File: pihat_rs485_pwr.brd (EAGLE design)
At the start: 56 x 65 mm, 36 parts, among them J1 RASPBERRYPI-40-PIN-GPIO_PTH_N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, Q1 MOSFET-N2N7002, Q2 MOSFET-N2N7002, Q3 MOSFET-N2N7002, Q4 MOSFET-P_SMD, Q5 BIPOLAR_TRANS_ARRAY, U1 MAX481CSA

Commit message: 11/29/17, changed PS, term blocks
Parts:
- 485: value TERMBLK_3PINNOSILK -> TERMBLK_3PINFEMALE; device UPenn:TERMBLK_3PIN_90_NOSILK -> UPenn:TERMBLK_FEMALE_3PIN_90_NOSILK
- J1: device UPenn:2X20 -> UPenn:PI_2X20
- PS1: value D24V22F5 -> R-78-E5.0; device UPenn:D24V22FX_FLAT -> UPenn:R-78-EXX
- moved S2 7.98 mm to (27.2, 21.3)
- moved R13 7.98 mm to (21.3, 23.1)
- moved R14 7.98 mm to (21.3, 19.6)
- moved R11 7.87 mm to (20.6, 34.0)
- moved R12 7.87 mm to (20.6, 28.7)
- moved 485 6.10 mm to (13.6, 27.9)
- moved RTCB 5.73 mm to (19.1, 16.0)
- moved R2 5.73 mm to (23.4, 16.0)
- moved R9 5.68 mm to (45.0, 22.6), turned to 0 degrees
- moved Q2 4.06 mm to (32.3, 27.7)
- moved R15 4.06 mm to (35.6, 36.8)
- moved C1 4.06 mm to (33.5, 17.3)
- moved Q1 4.06 mm to (45.7, 29.5)
- moved Q3 4.06 mm to (27.2, 27.7)
- moved R10 4.06 mm to (39.4, 36.3)
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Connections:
- net GND: now also 485.4
- net N$13: now also 485.5
- net N$25: now also 485.6
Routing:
- net N$27: track 19.1 -> 13.8 mm
- net N$3: track 53.4 -> 49.3 mm
- net N$22: track 56.9 -> 53.3 mm
- net N$2: track 16.0 -> 12.6 mm
- net 3.3V: track 89.7 -> 92.2 mm
- net N$25: track 31.6 -> 29.3 mm
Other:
- outline, holes or cut-outs redrawn
- board text added: "TX+"
- board text added: "TX-"
- board text removed: "EN"
- board text removed: "PG"

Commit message: 11/30/17, changes to silkscreen
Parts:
- moved PS1 2.54 mm to (17.8, 49.5)
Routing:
- net N$8: track 20.0 -> 17.4 mm
- net VIN: track 9.00 -> 11.4 mm
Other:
- board text added: "PIN11"
- board text added: "PIN15"
- board text added: "PIN15_CTRL"
- board text removed: "C"
- board text removed: "GPIO17"
- board text removed: "GPIO22"
- board text removed: "PIN_CTRL"

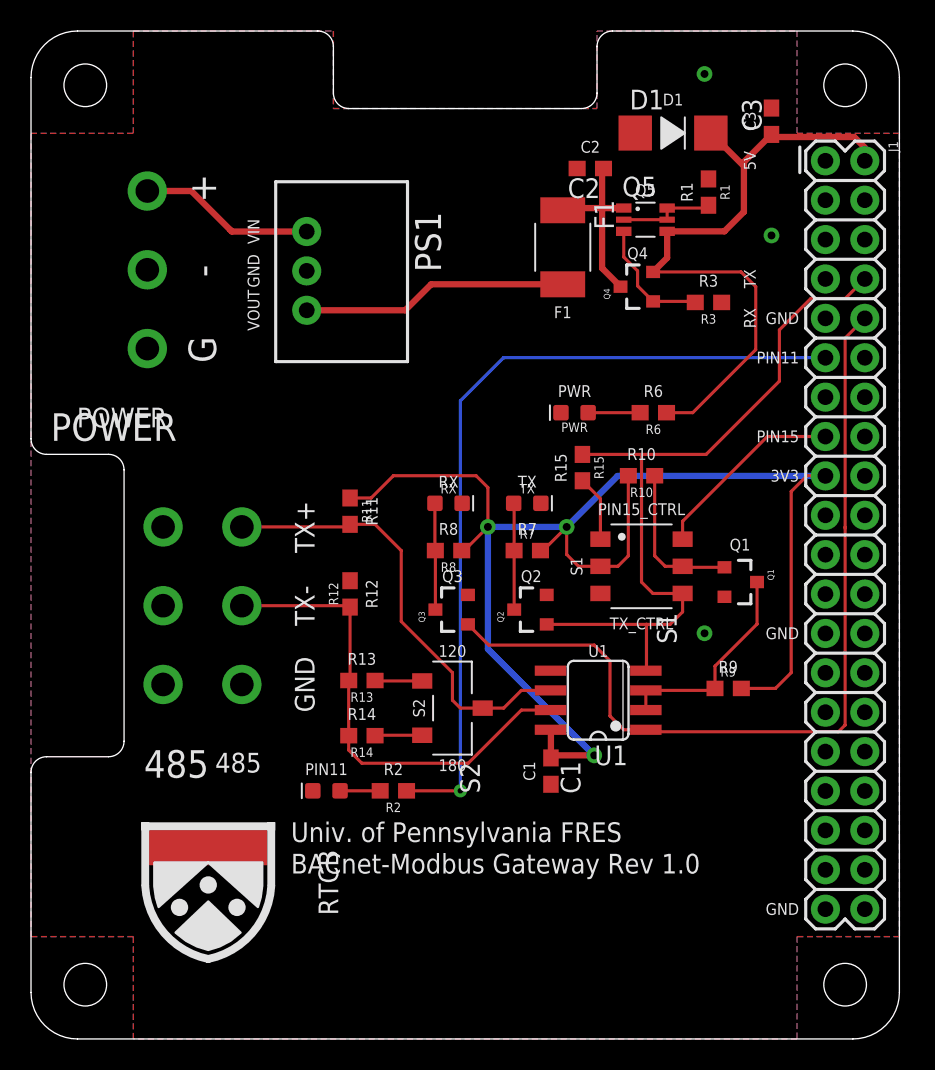
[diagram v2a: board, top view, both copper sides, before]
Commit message: 11/30/17, moved some parts, updated gerbers
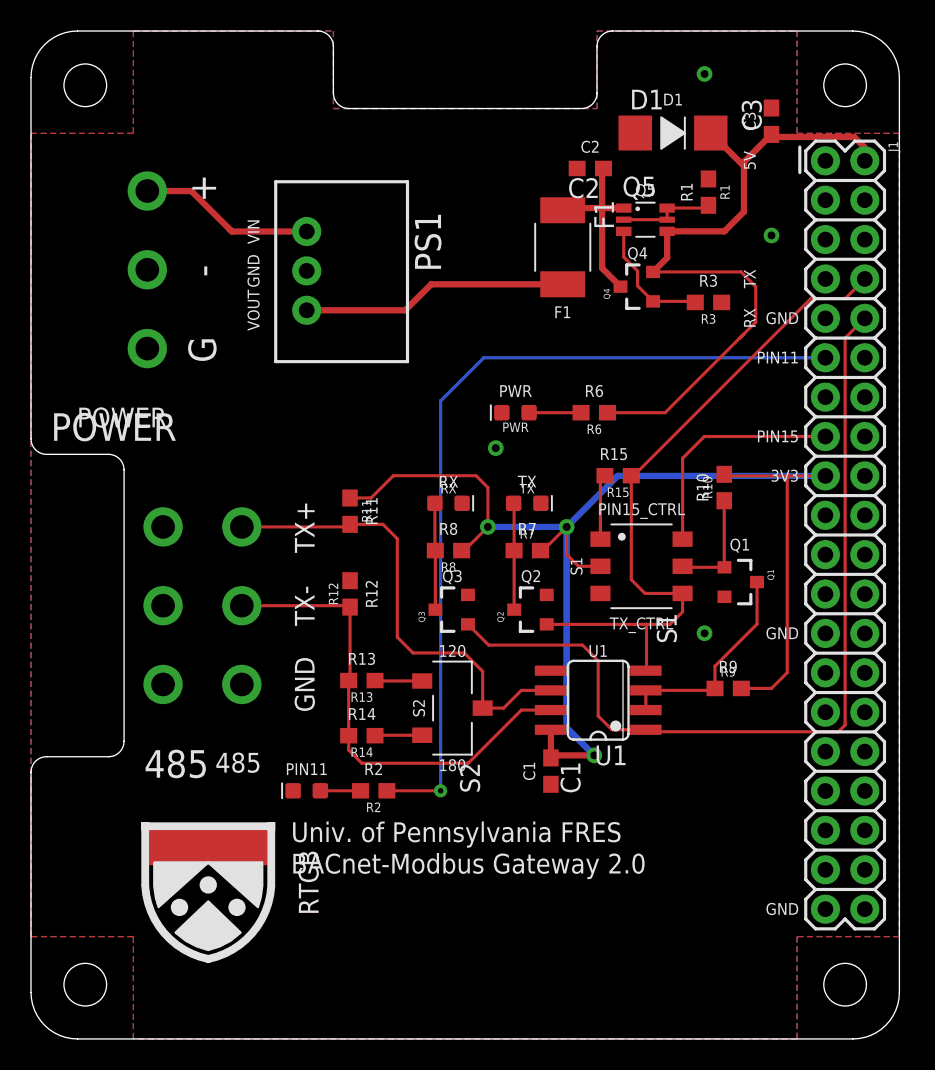
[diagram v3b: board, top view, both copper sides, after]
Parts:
- moved R10 5.39 mm to (44.7, 35.6), turned to 90 degrees
- moved PWR 3.81 mm to (31.2, 40.4)
- moved R6 3.81 mm to (36.3, 40.4)
- moved R15 2.36 mm to (37.9, 36.3), turned to 180 degrees
- moved R2 1.27 mm to (22.1, 16.0)
- moved RTCB 1.27 mm to (17.8, 16.0)
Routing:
- net N$3: track 49.3 -> 44.0 mm
- net 3.3V: track 92.2 -> 87.5 mm
- net 5V: track 42.9 -> 46.1 mm
- net N$26: track 10.1 -> 7.03 mm
- net N$2: track 12.6 -> 15.0 mm
- net N$25: track 29.3 -> 30.6 mm
- net N$22: track 53.3 -> 54.6 mm
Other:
- board text added: "BACnet-Modbus Gateway 2.0"
- board text removed: "BACnet-Modbus Gateway Rev 1.0"

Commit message: 1/4/18, moved D1 and C3, updated gerbers
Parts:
- moved C3 7.15 mm to (47.0, 52.1), turned to 0 degrees
- moved F1 3.81 mm to (30.5, 51.1)
- moved D1 2.30 mm to (43.7, 58.7)
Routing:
- net N$8: track 17.4 -> 13.6 mm
- net N$7: track 12.1 -> 15.9 mm
- net 5V: track 46.1 -> 45.0 mm
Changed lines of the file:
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@@
 <layers>
 <layer number="1" name="Top" color="4" fill="1" visible="yes" active="yes"/>
-<layer number="16" name="Bottom" color="1" fill="1" visible="no" active="yes"/>
+<layer number="16" name="Bottom" color="1" fill="1" visible="yes" active="yes"/>
 <layer number="17" name="Pads" color="2" fill="1" visible="yes" active="yes"/>
 <layer number="18" name="Vias" color="2" fill="1" visible="yes" active="yes"/>
@@
 <layer number="20" name="Dimension" color="15" fill="1" visible="yes" active="yes"/>
 <layer number="21" name="tPlace" color="7" fill="1" visible="yes" active="yes"/>
-<layer number="22" name="bPlace" color="7" fill="1" visible="no" active="yes"/>
+<layer number="22" name="bPlace" color="7" fill="1" visible="yes" active="yes"/>
 <layer number="23" name="tOrigins" color="15" fill="1" visible="yes" active="yes"/>
-<layer number="24" name="bOrigins" color="15" fill="1" visible="no" active="yes"/>
-<layer number="25" name="tNames" color="7" fill="1" visible="no" active="yes"/>
-<layer number="26" name="bNames" color="7" fill="1" visible="no" active="yes"/>
+<layer number="24" name="bOrigins" color="15" fill="1" visible="yes" active="yes"/>
+<layer number="25" name="tNames" color="7" fill="1" visible="yes" active="yes"/>
+<layer number="26" name="bNames" color="7" fill="1" visible="yes" active="yes"/>
 <layer number="27" name="tValues" color="7" fill="1" visible="no" active="yes"/>
 <layer number="28" name="bValues" color="7" fill="1" visible="no" active="yes"/>
@@
 <layer number="38" name="bTest" color="7" fill="1" visible="no" active="yes"/>
 <layer number="39" name="tKeepout" color="4" fill="11" visible="yes" active="yes"/>
-<layer number="40" name="bKeepout" color="1" fill="11" visible="no" active="yes"/>
+<layer number="40" name="bKeepout" color="1" fill="11" visible="yes" active="yes"/>
 <layer number="41" name="tRestrict" color="4" fill="10" visible="yes" active="yes"/>
-<layer number="42" name="bRestrict" color="1" fill="10" visible="no" active="yes"/>
+<layer number="42" name="bRestrict" color="1" fill="10" visible="yes" active="yes"/>
 <layer number="43" name="vRestrict" color="2" fill="10" visible="no" active="yes"/>
 <layer number="44" name="Drills" color="7" fill="1" visible="no" active="yes"/>
@@
 <layer number="49" name="Reference" color="7" fill="1" visible="no" active="yes"/>
 <layer number="50" name="dxf" color="7" fill="1" visible="no" active="no"/>
-<layer number="51" name="tDocu" color="14" fill="1" visible="no" active="yes"/>
-<layer number="52" name="bDocu" color="14" fill="1" visible="no" active="yes"/>
+<layer number="51" name="tDocu" color="14" fill="1" visible="yes" active="yes"/>
+<layer number="52" name="bDocu" color="14" fill="1" visible="yes" active="yes"/>
 <layer number="53" name="tGND_GNDA" color="7" fill="9" visible="no" active="no"/>
 <layer number="54" name="bGND_GNDA" color="1" fill="9" visible="no" active="no"/>
@@
 <text x="39.624" y="54.356" size="0.762" layer="21" font="vector" ratio="15" align="bottom-center">Q5</text>
 <text x="42.672" y="54.61" size="0.762" layer="21" font="vector" ratio="15" rot="R90" align="bottom-center">R1</text>
-<text x="41.402" y="60.198" size="0.762" layer="21" font="vector" ratio="15" align="bottom-center">D1</text>
-<text x="46.736" y="59.182" size="0.762" layer="21" font="vector" ratio="15" rot="R90" align="bottom-center">C3</text>
+<text x="43.688" y="60.452" size="0.762" layer="21" font="vector" ratio="15" align="bottom-center">D1</text>
+<text x="46.99" y="53.34" size="0.762" layer="21" font="vector" ratio="15" align="bottom-center">C3</text>
 <text x="36.068" y="57.15" size="0.762" layer="21" font="vector" ratio="15" align="bottom-center">C2</text>
-<text x="34.29" y="47.244" size="0.762" layer="21" font="vector" ratio="15" rot="R180" align="bottom-center">F1</text>
+<text x="30.48" y="47.244" size="0.762" layer="21" font="vector" ratio="15" rot="R180" align="bottom-center">F1</text>
 <text x="49.53" y="38.862" size="0.762" layer="21" font="vector" ratio="15" align="center-right">PIN15</text>
 <text x="49.53" y="36.322" size="0.762" layer="21" font="vector" ratio="15" align="center-right">3V3</text>
@@
 <element name="J1" library="UPenn" package="PI_2X20" value="RASPBERRYPI-40-PIN-GPIO_PTH_NO_SHROUND" x="52.5" y="32.5" rot="R270"/>
 <element name="Q4" library="UPenn" package="SOT23-3" value="MOSFET-P_SMD" x="39.116" y="48.514" rot="R90"/>
-<element name="F1" library="UPenn" package="1812_STD_BI" value="FUSE" x="34.29" y="51.054" rot="R270"/>
+<element name="F1" library="UPenn" package="1812_STD_BI" value="FUSE" x="30.48" y="51.054" rot="R270"/>
 <element name="Q5" library="UPenn" package="SOT363" value="BIPOLAR_TRANS_ARRAY" x="39.624" y="52.832"/>
-<element name="D1" library="UPenn" package="DO-214AA_UNI" value="DIODE_UNI" x="41.402" y="58.42"/>
-<element name="C3" library="resistor" library_urn="urn:adsk.eagle:library:348" package="C0603" package3d_urn="urn:adsk.eagle:package:26138/1" value="47 uF" x="47.752" y="59.182" rot="R90"/>
+<element name="D1" library="UPenn" package="DO-214AA_UNI" value="DIODE_UNI" x="43.688" y="58.674"/>
+<element name="C3" library="resistor" library_urn="urn:adsk.eagle:library:348" package="C0603" package3d_urn="urn:adsk.eagle:package:26138/1" value="47 uF" x="46.99" y="52.07"/>
 <element name="C2" library="resistor" library_urn="urn:adsk.eagle:library:348" package="C0603" package3d_urn="urn:adsk.eagle:package:26138/1" value="1.0 uF" x="36.068" y="56.134" rot="R180"/>
 <element name="R1" library="SparkFun-Resistors" package="0603" value="10K" x="43.688" y="54.61" rot="R270">
@@
 <contactref element="PS1" pad="GND"/>
 <via x="43.434" y="62.23" extent="1-16" drill="0.508"/>
-<via x="47.752" y="51.816" extent="1-16" drill="0.508"/>
+<via x="48.006" y="55.372" extent="1-16" drill="0.508"/>
 <via x="29.972" y="38.1" extent="1-16" drill="0.508"/>
 </signal>
@@
 <wire x1="41.024" y1="50.372" x2="41.024" y2="52.082" width="0.4064" layer="1"/>
 <wire x1="53.77" y1="57.482" x2="53.77" y2="56.63" width="0.4064" layer="1"/>
-<wire x1="53.086" y1="58.166" x2="53.77" y2="57.482" width="0.4064" layer="1"/>
-<wire x1="41.024" y1="52.082" x2="44.716" y2="52.082" width="0.4064" layer="1"/>
-<wire x1="44.716" y1="52.082" x2="45.974" y2="53.34" width="0.4064" layer="1"/>
-<wire x1="45.974" y1="53.34" x2="45.974" y2="56.2864" width="0.4064" layer="1"/>
-<wire x1="45.974" y1="56.2864" x2="43.8404" y2="58.42" width="0.4064" layer="1"/>
-<wire x1="45.974" y1="56.2864" x2="45.974" y2="56.554" width="0.4064" layer="1"/>
-<wire x1="45.974" y1="56.554" x2="47.752" y2="58.332" width="0.4064" layer="1"/>
-<wire x1="47.752" y1="58.332" x2="47.918" y2="58.166" width="0.4064" layer="1"/>
-<wire x1="47.918" y1="58.166" x2="53.086" y2="58.166" width="0.4064" layer="1"/>
+<wire x1="53.77" y1="57.482" x2="53.086" y2="58.166" width="0.4064" layer="1"/>
+<wire x1="41.024" y1="52.082" x2="46.128" y2="52.082" width="0.4064" layer="1"/>
 <wire x1="45.786" y1="49.464" x2="40.116" y2="49.464" width="0.2032" layer="1"/>
 <wire x1="45.786" y1="49.464" x2="46.736" y2="48.514" width="0.2032" layer="1"/>
 <contactref element="J1" pad="4"/>
 <wire x1="46.736" y1="48.514" x2="46.736" y2="46.228" width="0.2032" layer="1"/>
-<wire x1="46.736" y1="46.228" x2="45.974" y2="45.466" width="0.2032" layer="1"/>
-<wire x1="45.974" y1="45.466" x2="45.72" y2="45.212" width="0.2032" layer="1"/>
-<wire x1="45.974" y1="45.466" x2="40.894" y2="40.386" width="0.2032" layer="1"/>
+<wire x1="46.736" y1="46.228" x2="40.894" y2="40.386" width="0.2032" layer="1"/>
 <wire x1="40.894" y1="40.386" x2="37.172" y2="40.386" width="0.2032" layer="1"/>
+<wire x1="46.128" y1="52.082" x2="46.14" y2="52.07" width="0.4064" layer="1"/>
+<wire x1="46.14" y1="52.07" x2="46.14" y2="58.6604" width="0.4064" layer="1"/>
+<wire x1="46.1264" y1="58.674" x2="46.14" y2="58.6604" width="0.4064" layer="1"/>
+<wire x1="53.086" y1="58.166" x2="46.6344" y2="58.166" width="0.4064" layer="1"/>
+<wire x1="46.6344" y1="58.166" x2="46.1264" y2="58.674" width="0.4064" layer="1"/>
 <wire x1="53.77" y1="56.63" x2="53.77" y2="54.09" width="0" layer="19" extent="1-1"/>
 </signal>
@@
 <contactref element="C2" pad="1"/>
 <wire x1="38.224" y1="53.582" x2="36.83" y2="53.582" width="0.4064" layer="1"/>
-<wire x1="36.83" y1="53.582" x2="34.4304" y2="53.582" width="0.4064" layer="1"/>
-<wire x1="34.4304" y1="53.582" x2="34.29" y2="53.4416" width="0.2032" layer="1"/>
+<wire x1="36.83" y1="53.582" x2="30.6204" y2="53.582" width="0.4064" layer="1"/>
+<wire x1="30.6204" y1="53.582" x2="30.48" y2="53.4416" width="0.2032" layer="1"/>
 <wire x1="38.016" y1="48.514" x2="36.83" y2="49.7" width="0.4064" layer="1"/>
 <wire x1="36.83" y1="49.7" x2="36.83" y2="53.582" width="0.4064" layer="1"/>
@@
 <signal name="N$8">
 <contactref element="F1" pad="1"/>
-<wire x1="34.29" y1="48.6664" x2="34.1376" y2="48.514" width="0.4064" layer="1"/>
-<wire x1="25.8064" y1="48.6664" x2="34.29" y2="48.6664" width="0.4064" layer="1"/>
+<wire x1="30.48" y1="48.6664" x2="30.3276" y2="48.514" width="0.4064" layer="1"/>
+<wire x1="25.8064" y1="48.6664" x2="30.48" y2="48.6664" width="0.4064" layer="1"/>
 <wire x1="25.8064" y1="48.6664" x2="24.13" y2="46.99" width="0.4064" layer="1"/>
 <contactref element="PS1" pad="VOUT"/>

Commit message: 1/8/18, change R2 value from 680 to 510 to reduce parts
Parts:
- R2: value 680 -> 510
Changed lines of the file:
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@@
 <attribute name="VERSION" value="v01" x="0" y="46.99" size="1.778" layer="27" display="off"/>
 </element>
-<element name="R2" library="SparkFun-Resistors" package="0603" value="680" x="22.098" y="16.002" rot="R180">
+<element name="R2" library="SparkFun-Resistors" package="0603" value="510" x="22.098" y="16.002" rot="R180">
 <attribute name="PROD_ID" value=" " x="22.098" y="16.002" size="1.778" layer="27" rot="R180" display="off"/>
 <attribute name="VALUE" value=" " x="22.098" y="16.002" size="1.778" layer="27" rot="R180" display="off"/>
